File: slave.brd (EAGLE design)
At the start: 221.8 x 119.2 mm, 321 parts, among them J2 EB21A-06-D, J3 EB21A-06-D, J4 EB21A-06-D, J5 EB21A-06-D, J6 282837-9, J7 282837-9, J8 282837-9, J9 1715250000, Q1 DMN2056U-7, Q10 DMN2056U-7, Q11 DMN2056U-7, Q12 DMN2056U-7, Q13 DMN2056U-7, Q14 DMN2056U-7, Q15 DMN2056U-7, Q16 DMN2056U-7, Q17 DMN2056U-7, Q18 DMN2056U-7, Q19 DMN2056U-7, Q2 DMN2056U-7, Q20 DMN2056U-7, Q21 DMN2056U-7, Q22 DMN2056U-7, Q23 DMN2056U-7, Q24 DMN2056U-7, Q25 DMN2056U-7, Q26 DMN2056U-7, Q27 DMN2056U-7, Q28 DMN2056U-7, Q29 DMN2056U-7, Q3 DMN2056U-7, Q30 DMN2056U-7, Q31 DMN2056U-7, Q32 DMN2056U-7, Q33 DMN2056U-7, Q34 DMN2056U-7, Q35 DMN2056U-7, Q36 DMN2056U-7, Q37 DMN2056U-7, Q38 DMN2056U-7, Q39 DMN2056U-7, Q4 DMN2056U-7, Q40 DMN2056U-7, Q41 DMN2056U-7, Q42 DMN2056U-7, Q5 DMN2056U-7, Q7 DMN2056U-7, Q8 DMN2056U-7, Q9 DMN2056U-7, U2 AP2112K-3.3TRG1, U3 MCP23008-E/P, U4 MCP23008-E/P, U5 MCP23008-E/P, U6 MC74HCT4851ADR2G, U7 MC74HCT4851ADR2G, U8 MC74HCT4851ADR2G, U9 MC74HCT4851ADR2G

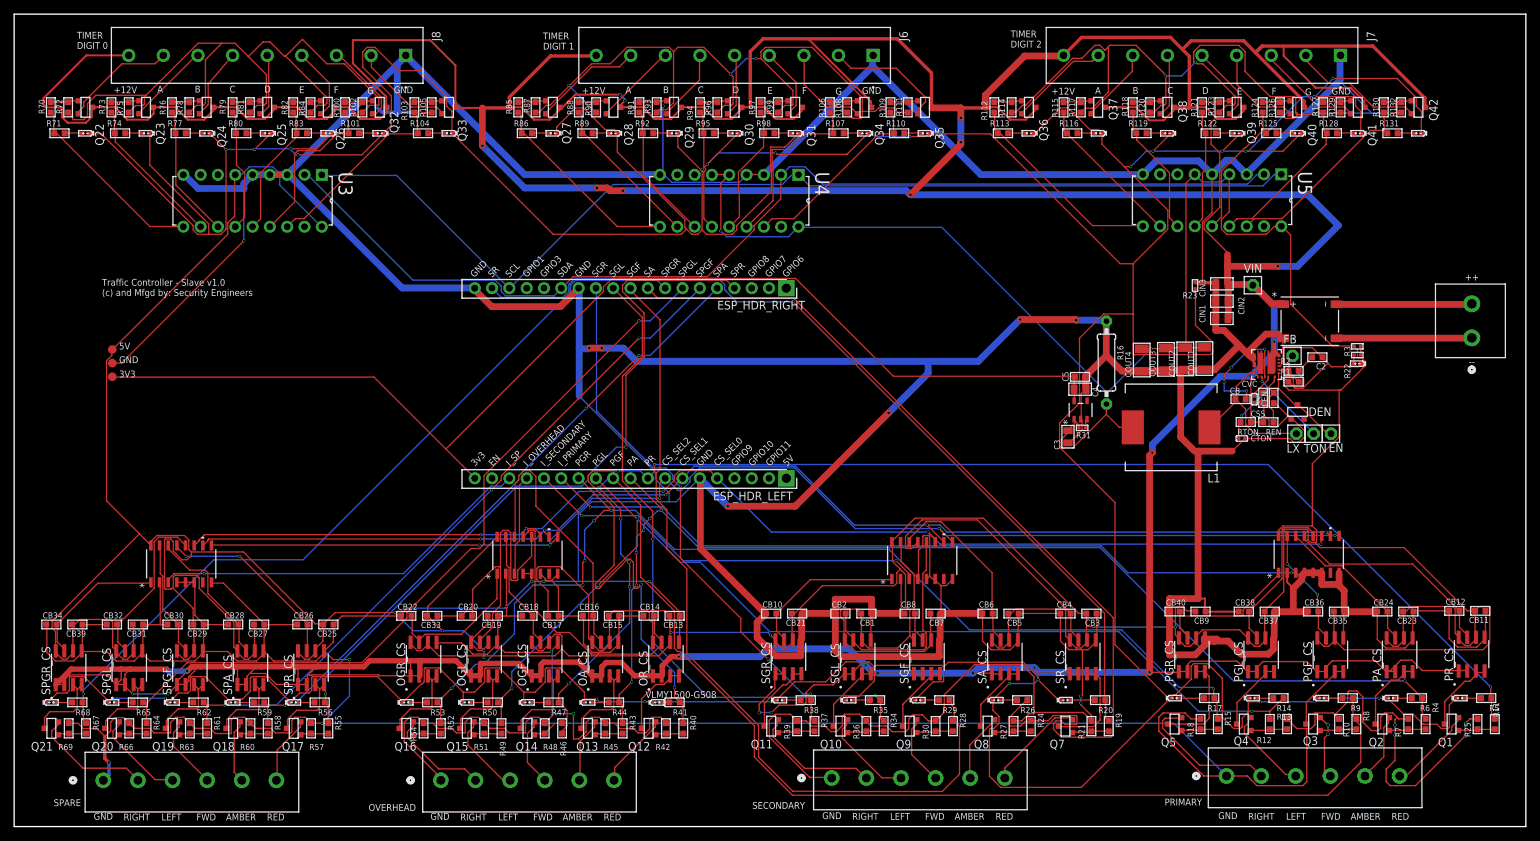
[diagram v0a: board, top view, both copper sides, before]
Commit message: finished v1.1 board and schematic design with Instrumentation amplifier and shunt
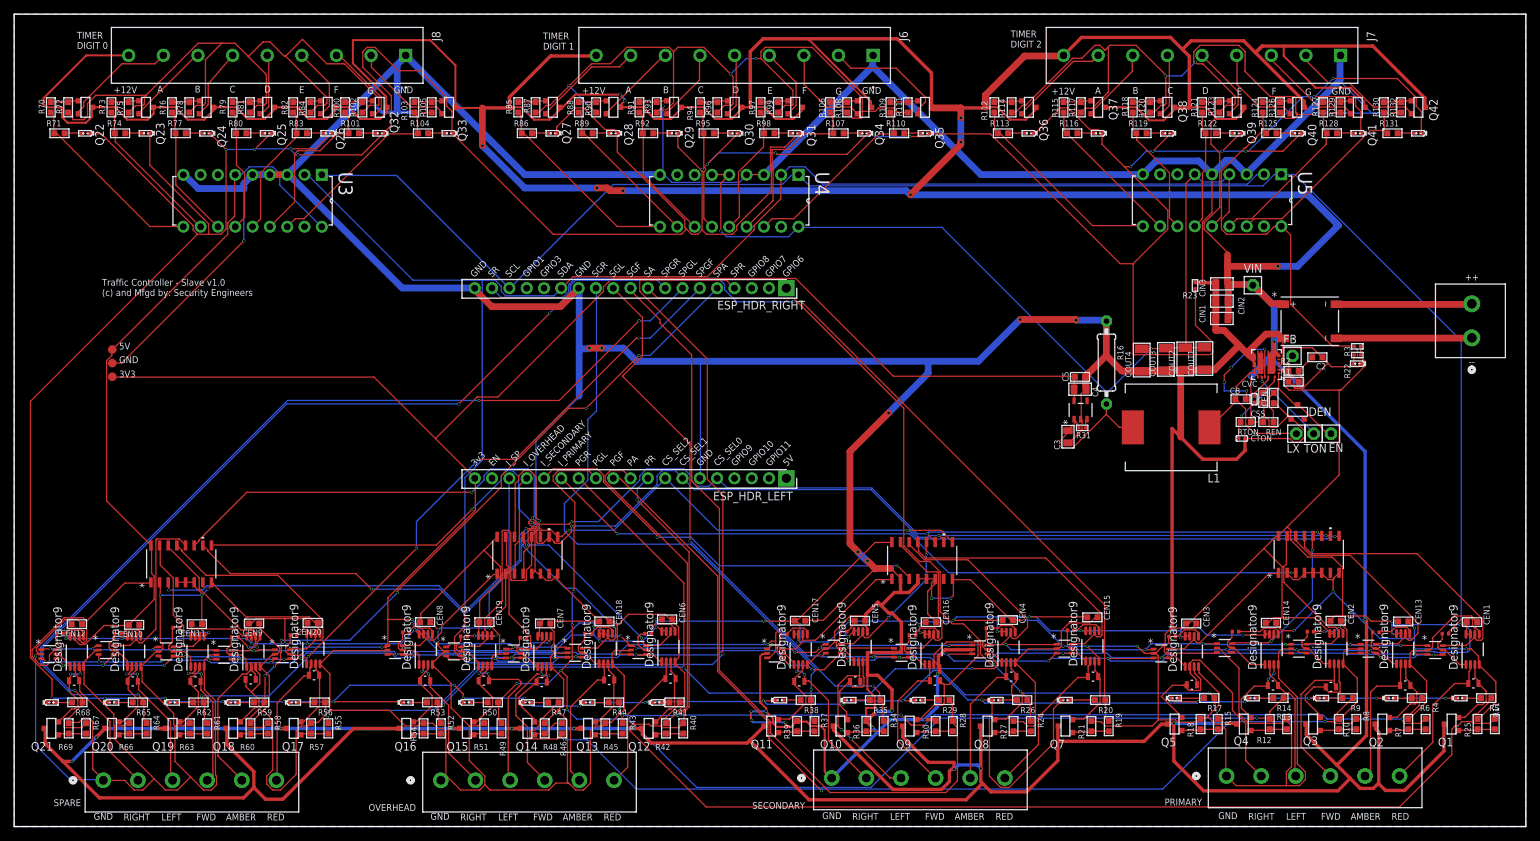
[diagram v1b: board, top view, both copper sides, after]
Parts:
- removed CB1, CB10, CB11, CB12, CB13, CB14, CB15, CB16, CB17, CB18, CB19, CB2, CB20, CB21, CB22, CB23, CB24, CB25, CB26, CB27, CB28, CB29, CB3, CB30, CB31, CB32, CB33, CB34, CB35, CB36, CB37, CB38, CB39, CB4, CB40, CB5, CB6, CB7, CB8, CB9: 100nF, OPL_Capacitor:C0603
- removed OA_CS, OGF_CS, OGL_CS, OGR_CS, OR_CS, PA_CS, PGF_CS, PGL_CS, PGR_CS, PR_CS, SA_CS, SGF_CS, SGL_CS, SGR_CS, SPA_CS, SPGF_CS, SPGL_CS, SPGR_CS, SPR_CS, SR_CS: ACS723LLCTR-10AU-T, ACS723LLCTR-10AU-T:SOIC127P600X175-8N
- added 3V1, 3V10, 3V11, 3V12, 3V13, 3V14, 3V15, 3V16, 3V17, 3V18, 3V19, 3V2, 3V21, 3V3, 3V4, 3V5, 3V6, 3V7, 3V8, 3V9: MCP40D17T-503E/LT, MCP40D17T-503E_LT:SC70-6_MC_MCH
- added CEN1, CEN10, CEN11, CEN12, CEN13, CEN14, CEN15, CEN16, CEN17, CEN18, CEN19, CEN2, CEN20, CEN3, CEN4, CEN5, CEN6, CEN7, CEN8, CEN9: 100nF, OPL_Capacitor:C0603
- added R133, R134, R135, R136, R137, R138, R139, R140, R141, R142, R143, R144, R145, R146, R147, R148, R149, R171, R32, R33: CR-02JL6----1K, CR-02JL6----1K:RES_CR-02_VKG
- added R150, R151, R152, R153, R154, R155, R156, R157, R158, R159, R160, R161, R162, R163, R164, R165, R166, R167, R168, R172: 1m, RLC16-R100JTP - 100mOhm:RES_RLC16_KYA
- added U1, U10, U11, U12, U13, U14, U15, U16, U17, U18, U19, U20, U21, U22, U23, U24, U25, U26, U27, U28: INA332AIDGKR, INA332AIDGKR:DGK0008A_N
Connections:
- removed net OA_IP-: OA_CS.3, OA_CS.4, Q13.P$3
- removed net OGF_IP-: OGF_CS.3, OGF_CS.4, Q14.P$3
- removed net OGL_IP-: OGL_CS.3, OGL_CS.4, Q15.P$3
- removed net OGR_IP-: OGR_CS.3, OGR_CS.4, Q16.P$3
- removed net OR_IP-: OR_CS.3, OR_CS.4, Q12.P$3
- removed net PA_IP-: PA_CS.3, PA_CS.4, Q2.P$3
- removed net PGF_IP-: PGF_CS.3, PGF_CS.4, Q3.P$3
- removed net PGL_IP-: PGL_CS.3, PGL_CS.4, Q4.P$3
- removed net PGR_IP-: PGR_CS.3, PGR_CS.4, Q5.P$3
- removed net PR_IP-: PR_CS.3, PR_CS.4, Q1.P$3
- removed net SA_IP-: Q8.P$3, SA_CS.3, SA_CS.4
- removed net SGF_IP-: Q9.P$3, SGF_CS.3, SGF_CS.4
- removed net SGL_IP-: Q10.P$3, SGL_CS.3, SGL_CS.4
- removed net SGR_IP-: Q11.P$3, SGR_CS.3, SGR_CS.4
- removed net SPA_IP-: Q18.P$3, SPA_CS.3, SPA_CS.4
- removed net SPGF_IP-: Q19.P$3, SPGF_CS.3, SPGF_CS.4
- removed net SPGL_IP-: Q20.P$3, SPGL_CS.3, SPGL_CS.4
- removed net SPGR_IP-: Q21.P$3, SPGR_CS.3, SPGR_CS.4
- removed net SPR_IP-: Q17.P$3, SPR_CS.3, SPR_CS.4
- removed net SR_IP-: Q7.P$3, SR_CS.3, SR_CS.4
- new net N$10: 3V2.5, R33.1, U10.1
- new net N$11: R33.2, U10.5
- new net N$12: 3V3.5, R133.1, U11.1
- new net N$13: R171.2, U19.5
- new net N$14: R133.2, U11.5
- new net N$16: 3V4.5, R134.1, U12.1
- new net N$17: R134.2, U12.5
- new net N$19: 3V5.5, R135.1, U13.1
- new net N$20: R135.2, U13.5
- new net N$22: 3V6.5, R136.1, U14.1
- new net N$23: R136.2, U14.5
- new net N$25: 3V7.5, R137.1, U15.1
- new net N$26: R137.2, U15.5
- new net N$28: 3V8.5, R138.1, U16.1
- new net N$29: R138.2, U16.5
- new net N$30: 3V9.5, R139.1, U17.1
- new net N$31: R139.2, U17.5
- new net N$32: 3V10.5, R140.1, U18.1
- new net N$33: R140.2, U18.5
- new net N$34: 3V11.5, R141.1, U20.1
- new net N$35: R141.2, U20.5
- new net N$36: 3V12.5, R142.1, U21.1
- new net N$37: R142.2, U21.5
- new net N$38: 3V13.5, R143.1, U22.1
- new net N$39: R143.2, U22.5
- new net N$4: 3V21.5, R171.1, U19.1
- new net N$40: 3V14.5, R144.1, U23.1
- new net N$41: R144.2, U23.5
- new net N$42: 3V15.5, R145.1, U24.1
- new net N$43: R145.2, U24.5
- new net N$44: 3V16.5, R146.1, U25.1
- new net N$45: R146.2, U25.5
- new net N$46: 3V17.5, R147.1, U26.1
- new net N$47: R147.2, U26.5
- new net N$48: 3V18.5, R148.1, U27.1
- new net N$49: R148.2, U27.5
- new net N$5: 3V1.5, R32.1, U1.1
- new net N$50: 3V19.5, R149.1, U28.1
- new net N$51: R149.2, U28.5
- new net N$6: R32.2, U1.5
- new net OA++: Q13.P$2, R165.2, U26.3
- new net OGF++: Q14.P$2, R166.2, U14.3
- new net OGL++: Q15.P$2, R167.2, U27.3
- new net OGR++: Q16.P$2, R168.2, U15.3
- new net OR++: Q12.P$2, R164.2, U13.3
- new net PA++: Q2.P$2, R150.2, U21.3
- new net PGF++: Q3.P$2, R151.2, U1.3
- new net PGL++: Q4.P$2, R152.2, U22.3
- new net PGR++: Q5.P$2, R153.2, U10.3
- new net PR++: Q1.P$2, R172.2, U19.3
- new net SA++: Q8.P$2, R155.2, U11.3
- new net SGF++: Q9.P$2, R156.2, U24.3
- new net SGL++: Q10.P$2, R157.2, U12.3
- new net SGR++: Q11.P$2, R158.2, U25.3
- new net SPA++: Q18.P$2, R160.2, U16.3
- new net SPGF++: Q19.P$2, R161.2, U18.3
- new net SPGL++: Q20.P$2, R162.2, U17.3
- new net SPGR++: Q21.P$2, R163.2, U20.3
- new net SPR++: Q17.P$2, R159.2, U28.3
- new net SR++: Q7.P$2, R154.2, U23.3
- net +5V: now also CEN1.2, CEN10.2, CEN11.2, CEN12.2, CEN13.2, CEN14.2, CEN15.2, CEN16.2, CEN17.2, CEN18.2, CEN19.2, CEN2.2, CEN20.2, CEN3.2, CEN4.2, CEN5.2, CEN6.2, CEN7.2, CEN8.2, CEN9.2, U1.7, U1.8, U10.7, U10.8, U11.7, U11.8, U12.7, U12.8, U13.7, U13.8, U14.7, U14.8, U15.7, U15.8, U16.7, U16.8, U17.7, U17.8, U18.7, U18.8, U19.7, U19.8, U20.7, U20.8, U21.7, U21.8, U22.7, U22.8, U23.7, U23.8, U24.7, U24.8, U25.7, U25.8, U26.7, U26.8, U27.7, U27.8, U28.7, U28.8; no longer CB1.2, CB11.2, CB13.2, CB15.2, CB17.2, CB19.2, CB21.2, CB23.2, CB25.2, CB27.2, CB29.2, CB3.2, CB31.2, CB33.2, CB35.2, CB37.2, CB39.2, CB5.2, CB7.2, CB9.2, OA_CS.6, OA_CS.8, OGF_CS.6, OGF_CS.8, OGL_CS.6, OGL_CS.8, OGR_CS.6, OGR_CS.8, OR_CS.6, OR_CS.8, PA_CS.6, PA_CS.8, PGF_CS.6, PGF_CS.8, PGL_CS.6, PGL_CS.8, PGR_CS.6, PGR_CS.8, PR_CS.6, PR_CS.8, SA_CS.6, SA_CS.8, SGF_CS.6, SGF_CS.8, SGL_CS.6, SGL_CS.8, SGR_CS.6, SGR_CS.8, SPA_CS.6, SPA_CS.8, SPGF_CS.6, SPGF_CS.8, SPGL_CS.6, SPGL_CS.8, SPGR_CS.6, SPGR_CS.8, SPR_CS.6, SPR_CS.8, SR_CS.6, SR_CS.8
- net 3V3: now also 3V1.1, 3V10.1, 3V11.1, 3V12.1, 3V13.1, 3V14.1, 3V15.1, 3V16.1, 3V17.1, 3V18.1, 3V19.1, 3V2.1, 3V21.1, 3V3.1, 3V4.1, 3V5.1, 3V6.1, 3V7.1, 3V8.1, 3V9.1
- net GND: now also 3V1.2, 3V10.2, 3V11.2, 3V12.2, 3V13.2, 3V14.2, 3V15.2, 3V16.2, 3V17.2, 3V18.2, 3V19.2, 3V2.2, 3V21.2, 3V3.2, 3V4.2, 3V5.2, 3V6.2, 3V7.2, 3V8.2, 3V9.2, CEN1.1, CEN11.1, CEN12.1, CEN13.1, CEN14.1, CEN15.1, CEN16.1, CEN17.1, CEN18.1, CEN19.1, CEN2.1, CEN20.1, CEN3.1, CEN4.1, CEN5.1, CEN6.1, CEN7.1, CEN8.1, CEN9.1, U1.4, U10.4, U11.4, U12.4, U13.4, U14.4, U15.4, U16.4, U17.4, U18.4, U19.4, U20.4, U21.4, U22.4, U23.4, U24.4, U25.4, U26.4, U27.4, U28.4; no longer CB1.1, CB10.1, CB11.1, CB12.1, CB13.1, CB14.1, CB15.1, CB16.1, CB17.1, CB18.1, CB19.1, CB2.1, CB20.1, CB21.1, CB22.1, CB23.1, CB24.1, CB25.1, CB26.1, CB27.1, CB28.1, CB29.1, CB3.1, CB30.1, CB31.1, CB32.1, CB33.1, CB34.1, CB35.1, CB36.1, CB37.1, CB38.1, CB39.1, CB4.1, CB40.1, CB5.1, CB6.1, CB7.1, CB8.1, CB9.1, OA_CS.5, OGF_CS.5, OGL_CS.5, OGR_CS.5, OR_CS.5, PA_CS.5, PGF_CS.5, PGL_CS.5, PGR_CS.5, PR_CS.5, SA_CS.5, SGF_CS.5, SGL_CS.5, SGR_CS.5, SPA_CS.5, SPGF_CS.5, SPGL_CS.5, SPGR_CS.5, SPR_CS.5, SR_CS.5
- net I_OA: now also 3V17.6, U26.6; no longer CB16.2, OA_CS.7
- net I_OGF: now also 3V6.6, U14.6; no longer CB18.2, OGF_CS.7
- net I_OGL: now also 3V18.6, U27.6; no longer CB20.2, OGL_CS.7
- net I_OGR: now also 3V7.6, U15.6; no longer CB22.2, OGR_CS.7
- net I_OR: now also 3V5.6, U13.6; no longer CB14.2, OR_CS.7
- net I_PA: now also 3V12.6, U21.6; no longer CB24.2, PA_CS.7
- net I_PGF: now also 3V1.6, U1.6; no longer CB36.2, PGF_CS.7
- net I_PGL: now also 3V13.6, U22.6; no longer CB38.2, PGL_CS.7
- net I_PGR: now also 3V2.6, U10.6; no longer CB40.2, PGR_CS.7
- net I_PR: now also 3V21.6, U19.6; no longer CB12.2, PR_CS.7
- net I_SA: now also 3V3.6, U11.6; no longer CB6.2, SA_CS.7
- net I_SGF: now also 3V15.6, U24.6; no longer CB8.2, SGF_CS.7
- net I_SGL: now also 3V4.6, U12.6; no longer CB2.2, SGL_CS.7
- net I_SGR: now also 3V16.6, U25.6; no longer CB10.2, SGR_CS.7
- net I_SPA: now also 3V8.6, U16.6; no longer CB28.2, SPA_CS.7
- net I_SPGF: now also 3V10.6, U18.6; no longer CB30.2, SPGF_CS.7
- net I_SPGL: now also 3V9.6, U17.6; no longer CB32.2, SPGL_CS.7
- net I_SPGR: now also 3V11.6, U20.6; no longer CB34.2, SPGR_CS.7
- net I_SPR: now also 3V19.6, U28.6; no longer CB26.2, SPR_CS.7
- net I_SR: now also 3V14.6, U23.6; no longer CB4.2, SR_CS.7
- net OA+: now also R165.1, U26.2; no longer Q13.P$2
- net OGF+: now also R166.1, U14.2; no longer Q14.P$2
- net OGL+: now also R167.1, U27.2; no longer Q15.P$2
- net OGR+: now also R168.1, U15.2; no longer Q16.P$2
- net OR+: now also R164.1, U13.2; no longer Q12.P$2
- net PA+: now also R150.1, U21.2; no longer Q2.P$2
- net PGF+: now also R151.1, U1.2; no longer Q3.P$2
- net PGL+: now also R152.1, U22.2; no longer Q4.P$2
- net PGR+: now also R153.1, U10.2; no longer Q5.P$2
- net PR+: now also R172.1, U19.2; no longer Q1.P$2
- net SA+: now also R155.1, U11.2; no longer Q8.P$2
- net SCL: now also 3V1.3, 3V10.3, 3V11.3, 3V12.3, 3V13.3, 3V14.3, 3V15.3, 3V16.3, 3V17.3, 3V18.3, 3V19.3, 3V2.3, 3V21.3, 3V3.3, 3V4.3, 3V5.3, 3V6.3, 3V7.3, 3V8.3, 3V9.3
- net SDA: now also 3V1.4, 3V10.4, 3V11.4, 3V12.4, 3V13.4, 3V14.4, 3V15.4, 3V16.4, 3V17.4, 3V18.4, 3V19.4, 3V2.4, 3V21.4, 3V3.4, 3V4.4, 3V5.4, 3V6.4, 3V7.4, 3V8.4, 3V9.4
- net SGF+: now also R156.1, U24.2; no longer Q9.P$2
- net SGL+: now also R157.1, U12.2; no longer Q10.P$2
- net SGR+: now also R158.1, U25.2; no longer Q11.P$2
- net SPA+: now also R160.1, U16.2; no longer Q18.P$2
- net SPGF+: now also R161.1, U18.2; no longer Q19.P$2
- net SPGL+: now also R162.1, U17.2; no longer Q20.P$2
- net SPGR+: now also R163.1, U20.2; no longer Q21.P$2
- net SPR+: now also R159.1, U28.2; no longer Q17.P$2
- net SR+: now also R154.1, U23.2; no longer Q7.P$2
- net VIN: now also Q1.P$3, Q10.P$3, Q11.P$3, Q12.P$3, Q13.P$3, Q14.P$3, Q15.P$3, Q16.P$3, Q17.P$3, Q18.P$3, Q19.P$3, Q2.P$3, Q20.P$3, Q21.P$3, Q3.P$3, Q4.P$3, Q5.P$3, Q7.P$3, Q8.P$3, Q9.P$3; no longer OA_CS.1, OA_CS.2, OGF_CS.1, OGF_CS.2, OGL_CS.1, OGL_CS.2, OGR_CS.1, OGR_CS.2, OR_CS.1, OR_CS.2, PA_CS.1, PA_CS.2, PGF_CS.1, PGF_CS.2, PGL_CS.1, PGL_CS.2, PGR_CS.1, PGR_CS.2, PR_CS.1, PR_CS.2, SA_CS.1, SA_CS.2, SGF_CS.1, SGF_CS.2, SGL_CS.1, SGL_CS.2, SGR_CS.1, SGR_CS.2, SPA_CS.1, SPA_CS.2, SPGF_CS.1, SPGF_CS.2, SPGL_CS.1, SPGL_CS.2, SPGR_CS.1, SPGR_CS.2, SPR_CS.1, SPR_CS.2, SR_CS.1, SR_CS.2
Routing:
- net SCL: track 156.0 -> 515.4 mm, vias 0 -> 21
- net SDA: track 160.5 -> 465.5 mm, vias 0 -> 26
- net 3V3: track 172.0 -> 452.8 mm, vias 0 -> 23
- net +5V: track 957.9 -> 772.4 mm, vias 10 -> 31
- net VIN: track 1050.7 -> 1109.8 mm
- net JP2: track 876.4 -> 840.8 mm, vias 25 -> 35
- net SA: track 136.2 -> 100.6 mm, vias 0 -> 2
- net SPR: track 108.8 -> 139.3 mm, vias 2 -> 3
- net GND: track 2036.8 -> 2006.6 mm, vias 37 -> 48
- net SGF++: track 0.00 -> 26.1 mm
- net SPGL: track 114.2 -> 139.3 mm, vias 1 -> 3
- net PGL: track 155.6 -> 174.4 mm, vias 4 -> 6
- net SPGR: track 116.5 -> 134.1 mm, vias 1 -> 3
- net PGR++: track 0.00 -> 15.7 mm
- net SR_IP-: track 14.9 -> 0.00 mm
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- added copper zone on layer 1, net GND
- added copper zone on layer 16, net GND

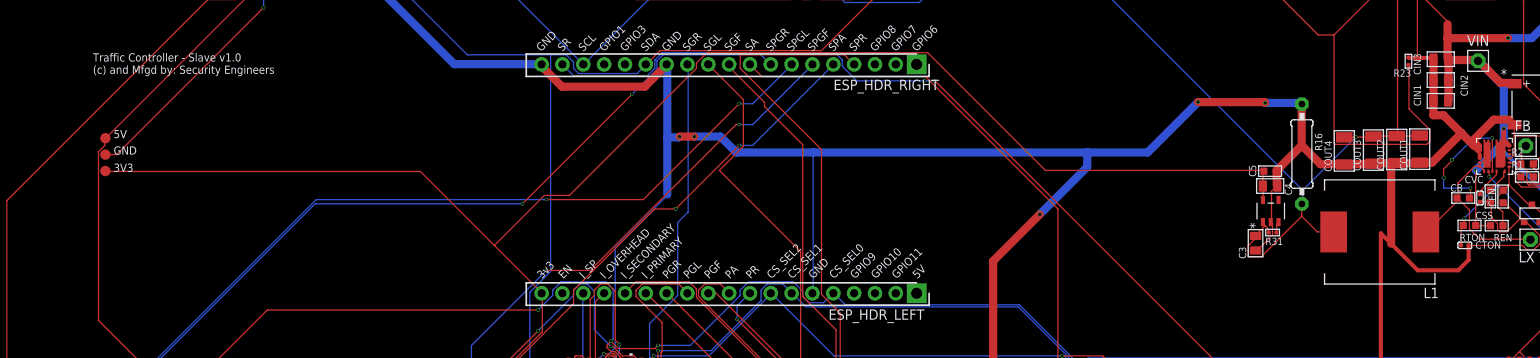
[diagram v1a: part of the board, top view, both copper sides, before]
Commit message: updated RTON 781.25k resistor with series of 698k and 82.5k resistors, generated gerber and bom, cpl files
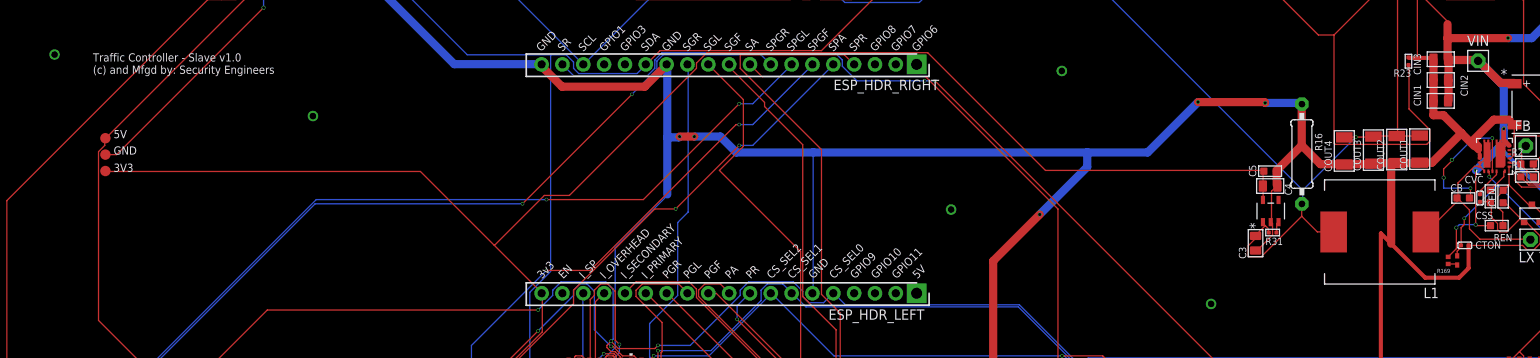
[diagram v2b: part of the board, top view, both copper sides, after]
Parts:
- removed RTON: 781.25k, OPL_Resistor:R0603
- added R169: RC0402FR-07698KL, RC0402FR-07698KL:RESC1005X40N
- added R170: RC0402FR-0782K5L, RC0402FR-0782K5L:RC0402N_YAG
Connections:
- new net N$52: R169.1, R170.2
- net TON: now also R170.1; no longer RTON.1
- net VIN: now also R169.2; no longer RTON.2
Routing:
- net VIN: track 1109.8 -> 1116.3 mm, vias 24 -> 26
- net TON: track 20.8 -> 22.3 mm
- net GND: track 2006.6 -> 2008.0 mm, vias 48 -> 53
- net N$52: track 0.00 -> 1.15 mm

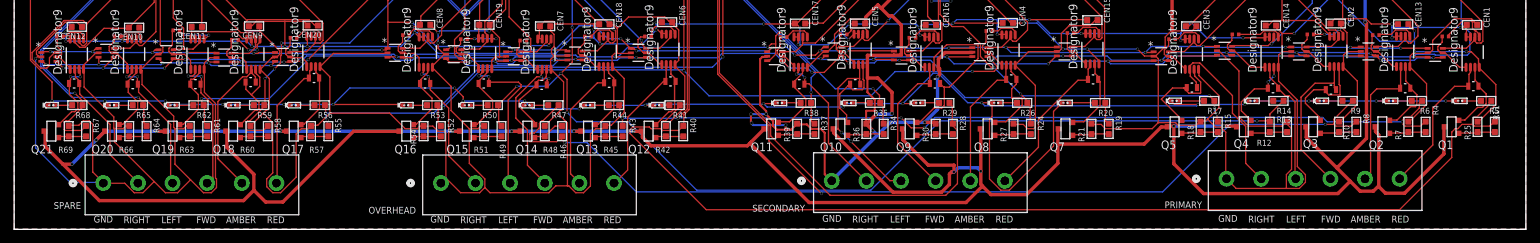
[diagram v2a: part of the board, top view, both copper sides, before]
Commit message: added new 100 mOhm shunt resistor for current sensing
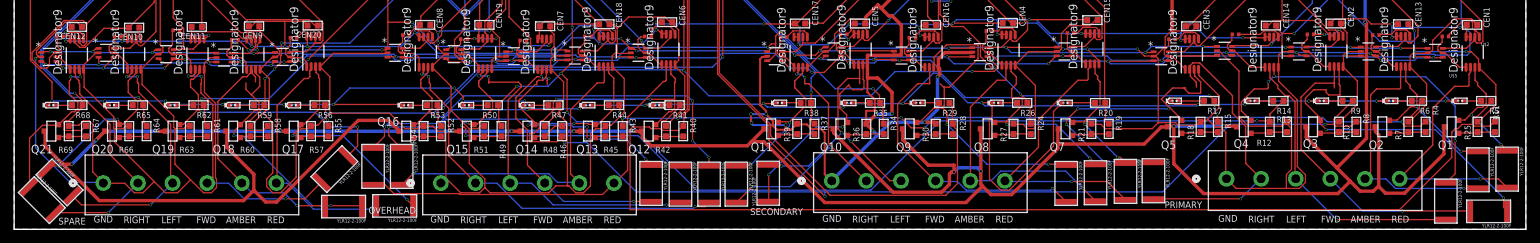
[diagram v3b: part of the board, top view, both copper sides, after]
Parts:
- removed R150, R151, R152, R153, R154, R155, R156, R157, R158, R159, R160, R161, R162, R163, R164, R165, R166, R167, R168, R172: 1m, RLC16-R100JTP - 100mOhm:RES_RLC16_KYA
- added U$1, U$10, U$11, U$12, U$13, U$14, U$15, U$16, U$17, U$18, U$19, U$2, U$20, U$21, U$4, U$5, U$6, U$7, U$8, U$9: YLR12-2-100F, YLR12-2-100F:YLR12-2-100F
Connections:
- net OA+: now also U$15.P$2; no longer R165.1
- net OA++: now also U$15.P$1; no longer R165.2
- net OGF+: now also U$14.P$2; no longer R166.1
- net OGF++: now also U$14.P$1; no longer R166.2
- net OGL+: now also U$13.P$2; no longer R167.1
- net OGL++: now also U$13.P$1; no longer R167.2
- net OGR+: now also U$12.P$2; no longer R168.1
- net OGR++: now also U$12.P$1; no longer R168.2
- net OR+: now also U$16.P$2; no longer R164.1
- net OR++: now also U$16.P$1; no longer R164.2
- net PA+: now also U$2.P$2; no longer R150.1
- net PA++: now also U$2.P$1; no longer R150.2
- net PGF+: now also U$4.P$2; no longer R151.1
- net PGF++: now also U$4.P$1; no longer R151.2
- net PGL+: now also U$5.P$2; no longer R152.1
- net PGL++: now also U$5.P$1; no longer R152.2
- net PGR+: now also U$6.P$2; no longer R153.1
- net PGR++: now also U$6.P$1; no longer R153.2
- net PR+: now also U$1.P$2; no longer R172.1
- net PR++: now also U$1.P$1; no longer R172.2
- net SA+: now also U$8.P$2; no longer R155.1
- net SA++: now also U$8.P$1; no longer R155.2
- net SGF+: now also U$9.P$2; no longer R156.1
- net SGF++: now also U$9.P$1; no longer R156.2
- net SGL+: now also U$10.P$2; no longer R157.1
- net SGL++: now also U$10.P$1; no longer R157.2
- net SGR+: now also U$11.P$2; no longer R158.1
- net SGR++: now also U$11.P$1; no longer R158.2
- net SPA+: now also U$18.P$2; no longer R160.1
- net SPA++: now also U$18.P$1; no longer R160.2
- net SPGF+: now also U$19.P$2; no longer R161.1
- net SPGF++: now also U$19.P$1; no longer R161.2
- net SPGL+: now also U$20.P$2; no longer R162.1
- net SPGL++: now also U$20.P$1; no longer R162.2
- net SPGR+: now also U$21.P$2; no longer R163.1
- net SPGR++: now also U$21.P$1; no longer R163.2
- net SPR+: now also U$17.P$2; no longer R159.1
- net SPR++: now also U$17.P$1; no longer R159.2
- net SR+: now also U$7.P$2; no longer R154.1
- net SR++: now also U$7.P$1; no longer R154.2
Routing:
- net OGR++: track 11.1 -> 61.9 mm, vias 0 -> 4
- net OR++: track 10.6 -> 59.0 mm, vias 0 -> 4
- net PGL++: track 11.5 -> 51.7 mm, vias 2 -> 3
- net OGL++: track 11.0 -> 48.2 mm, vias 0 -> 4
- net OR+: track 20.8 -> 57.4 mm
- net OGR+: track 20.7 -> 56.9 mm, vias 2 -> 3
- net OA++: track 10.3 -> 45.2 mm, vias 0 -> 2
- net PGF++: track 14.5 -> 48.6 mm, vias 0 -> 2
- net PGR++: track 15.7 -> 46.9 mm, vias 0 -> 4
- net SPGF++: track 10.8 -> 40.2 mm, vias 0 -> 2
- net OA+: track 20.3 -> 47.6 mm, vias 0 -> 1
- net OGL+: track 24.1 -> 50.4 mm, vias 2 -> 3
- net SPA++: track 12.9 -> 38.0 mm, vias 0 -> 2
- net PGL+: track 18.3 -> 42.8 mm, vias 0 -> 1
- net SPR++: track 10.1 -> 34.2 mm, vias 0 -> 2
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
